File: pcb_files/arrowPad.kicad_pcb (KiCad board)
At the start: 2 copper layers, 76.2 x 64.8 mm, 30 parts, among them J1 AudioJack3_Ground, J2 AudioJack3_Ground, K1 KEYSW, K2 KEYSW, K3 KEYSW, K4 KEYSW, K5 KEYSW, K6 KEYSW, K7 KEYSW, K8 KEYSW, K9 KEYSW, U1 ProMicro, U2 NRF24L01_Breakout, U3 ADG417BN

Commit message: started reworking board
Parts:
- removed REF** (x4): MountingHole_3.5mm, MountingHole:MountingHole_3.5mm
- added U4: AMS1117-3.3, promicro:AMS1117flipped, F.Cu at (38.7, 90.8)
- J1, J2: footprint Connector_PinHeader_2.54mm:PinHeader_1x04_P2.54mm_Vertical -> SJ1-3514-SMT:CUI_SJ1-3514-SMT
- moved J1 15.8 mm to (38.1, 123.8), turned to 0 degrees
- moved J2 6.56 mm to (102.9, 128.9), turned to 180 degrees
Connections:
- U2 pad 2: Net-(J1-Pad3) -> Net-(U2-Pad2)
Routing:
- net Net-(J1-Pad2): track 145.8 -> 147.3 mm, vias 0 -> 2
- net Net-(J1-Pad1): track 151.5 -> 150.1 mm, vias 2 -> 0
- removed copper zone on F.Cu, net /GND1

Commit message: v2
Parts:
- removed J1, J2: AudioJack3_Ground, SJ1-3514-SMT:CUI_SJ1-3514-SMT
- removed R1: R, keyboard_parts:D_SOD123_axial
- added D11: D, keyboard_parts:D_SOD123_axial, F.Cu at (167.1, 112.6)
- added D12: D, keyboard_parts:D_SOD123_axial, F.Cu at (184.9, 112.0)
- added D13: D, keyboard_parts:D_SOD123_axial, F.Cu at (130.3, 131.1)
- added D14: D, keyboard_parts:D_SOD123_axial, F.Cu at (149.4, 131.7)
- added D15: D, keyboard_parts:D_SOD123_axial, F.Cu at (167.8, 132.3)
- added D16: D, keyboard_parts:D_SOD123_axial, F.Cu at (186.2, 131.1)
- added K10: KEYSW, keyswitches:PG1350_socket, F.Cu at (149.9, 102.9)
- added K11: KEYSW, keyswitches:PG1350_socket, F.Cu at (168.9, 102.9)
- added K12: KEYSW, keyswitches:PG1350_socket, F.Cu at (188.0, 102.9)
- added K13: KEYSW, keyswitches:PG1350_socket, F.Cu at (130.8, 121.9)
- added K14: KEYSW, keyswitches:PG1350_socket, F.Cu at (149.9, 121.9)
- added K15: KEYSW, keyswitches:PG1350_socket, F.Cu at (168.9, 121.9)
- added K16: KEYSW, keyswitches:PG1350_socket, F.Cu at (188.0, 121.9)
- D10: value LED -> D; footprint Connector_PinHeader_2.54mm:PinHeader_1x02_P2.54mm_Vertical -> keyboard_parts:D_SOD123_axial
- U1: footprint Transformer_SMD:proMicrov6 -> promicro:ProMicro
- moved K4 143.6 mm to (188.0, 64.8)
- moved D4 143.3 mm to (188.0, 74.9)
- moved BT1 126.4 mm to (179.1, 43.2)
- moved K8 126.0 mm to (188.0, 83.8)
- moved D7 125.7 mm to (169.0, 93.0)
- moved K7 125.5 mm to (168.9, 83.8)
- moved D8 124.2 mm to (186.2, 93.6)
- moved D10 107.5 mm to (148.7, 112.0), turned to 180 degrees
- moved U3 94.3 mm to (162.6, 54.6)
- moved D2 88.1 mm to (148.6, 61.0)
- moved D1 87.6 mm to (129.5, 61.0)
- moved K3 84.6 mm to (168.9, 64.8)
- moved D3 84.3 mm to (168.9, 74.9)
- moved K2 84.1 mm to (149.9, 64.8)
- moved K1 83.5 mm to (130.8, 64.8)
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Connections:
- net Net-(J1-Pad3) renamed /VCC1
- D10 pad 1: /GND1 -> /Row3
- D4 pad 1: /Row2 -> /Row1
- D7 pad 1: /Row3 -> /Row2
- D8 pad 1: /Row3 -> /Row2
- K4 pad 1: /Col1 -> /Col4
- K5 pad 1: /Col2 -> /Col1
- K6 pad 1: /Col3 -> /Col2
- K7 pad 1: /Col1 -> /Col3
- K8 pad 1: /Col2 -> /Col4
- K9 pad 1: /Col3 -> /Col1
- U1 pad 6: /Col1 -> Net-(J1-Pad2)
- U1 pad 7: Net-(R1-Pad1) -> /Col1
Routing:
- net Net-(U1-Pad1): track 150.1 -> 0.00 mm
- net Net-(U1-Pad2): track 147.3 -> 0.00 mm, vias 2 -> 0
- net /Col2: track 115.3 -> 0.00 mm, vias 5 -> 0
- net /Col1: track 100.8 -> 0.00 mm, vias 2 -> 0
- net /VCC1: track 90.8 -> 0.00 mm, vias 4 -> 0
- net /Row3: track 86.6 -> 0.00 mm, vias 1 -> 0
- net /RAW1: track 81.0 -> 0.00 mm, vias 1 -> 0
- net /Row2: track 56.4 -> 0.00 mm
- net Net-(R1-Pad1): track 49.9 -> 0.00 mm
- net /Col3: track 49.1 -> 0.00 mm, vias 3 -> 0
- net /Row1: track 47.5 -> 0.00 mm
- net Net-(U1-Pad18): track 23.8 -> 0.00 mm, vias 1 -> 0
- net Net-(U1-Pad15): track 22.6 -> 0.00 mm, vias 1 -> 0
- net Net-(U1-Pad17): track 22.3 -> 0.00 mm
- net Net-(U1-Pad16): track 21.3 -> 0.00 mm
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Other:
- board outline removed

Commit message: updated
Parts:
- moved BT1 28.7 mm to (151.1, 49.5)
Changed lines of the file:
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@@
   )
   (module Connector_PinHeader_2.54mm:PinHeader_1x02_P2.54mm_Vertical (layer F.Cu)
-    (at 179.07 43.18)
+    (at 151.13 49.53)
     (descr "Through hole straight pin header, 1x02, 2.54mm pitch, single row")
     (tags "Through hole pin header THT 1x02 2.54mm single row")

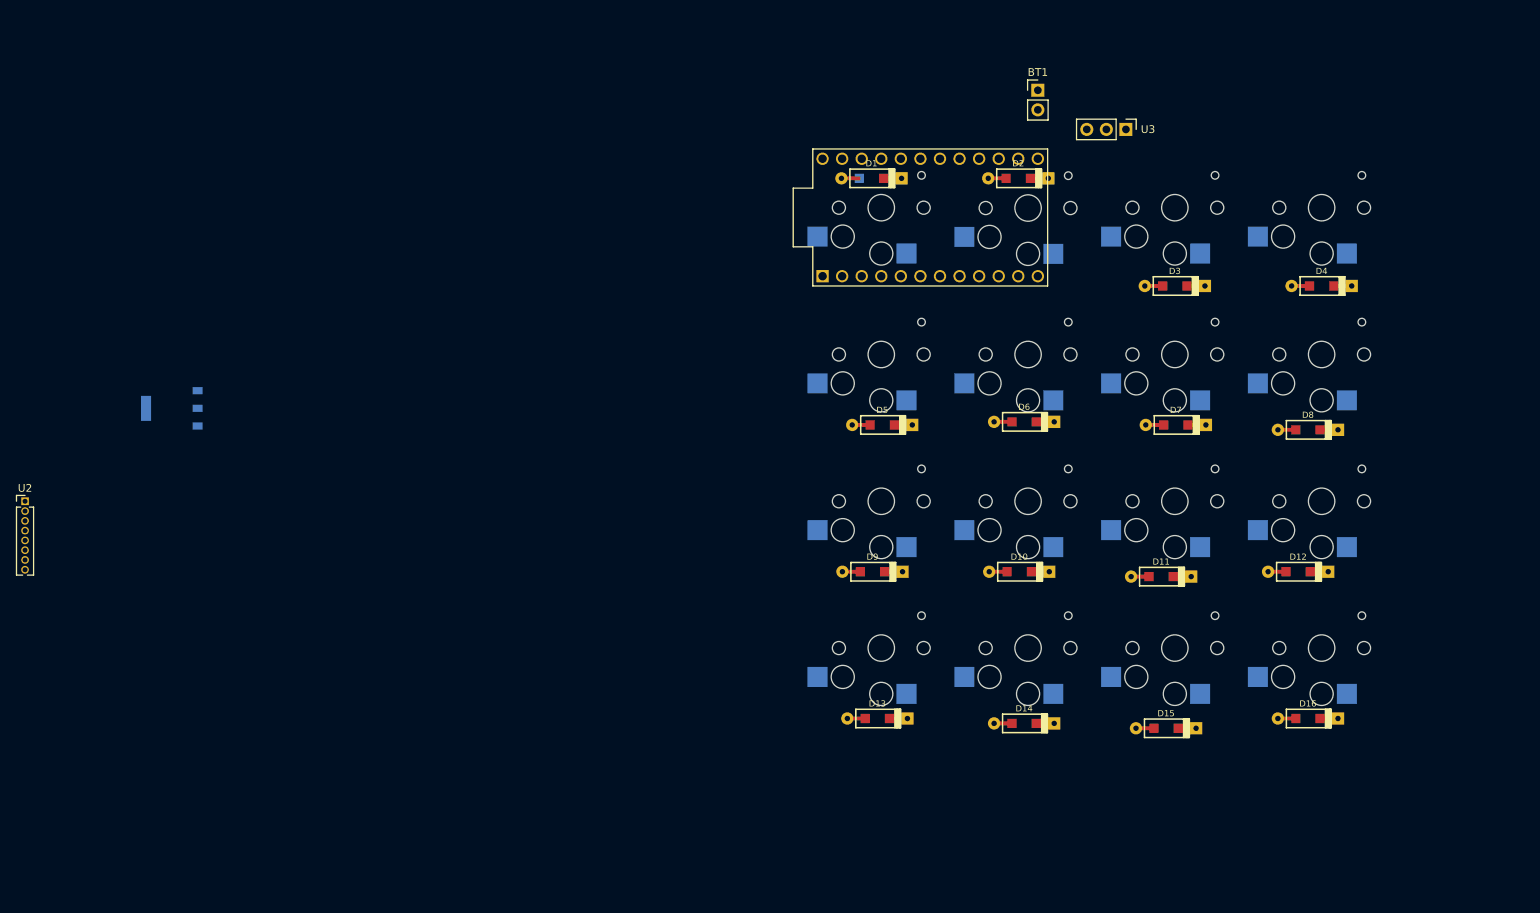
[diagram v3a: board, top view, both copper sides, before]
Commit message: switch and diode pcb layout
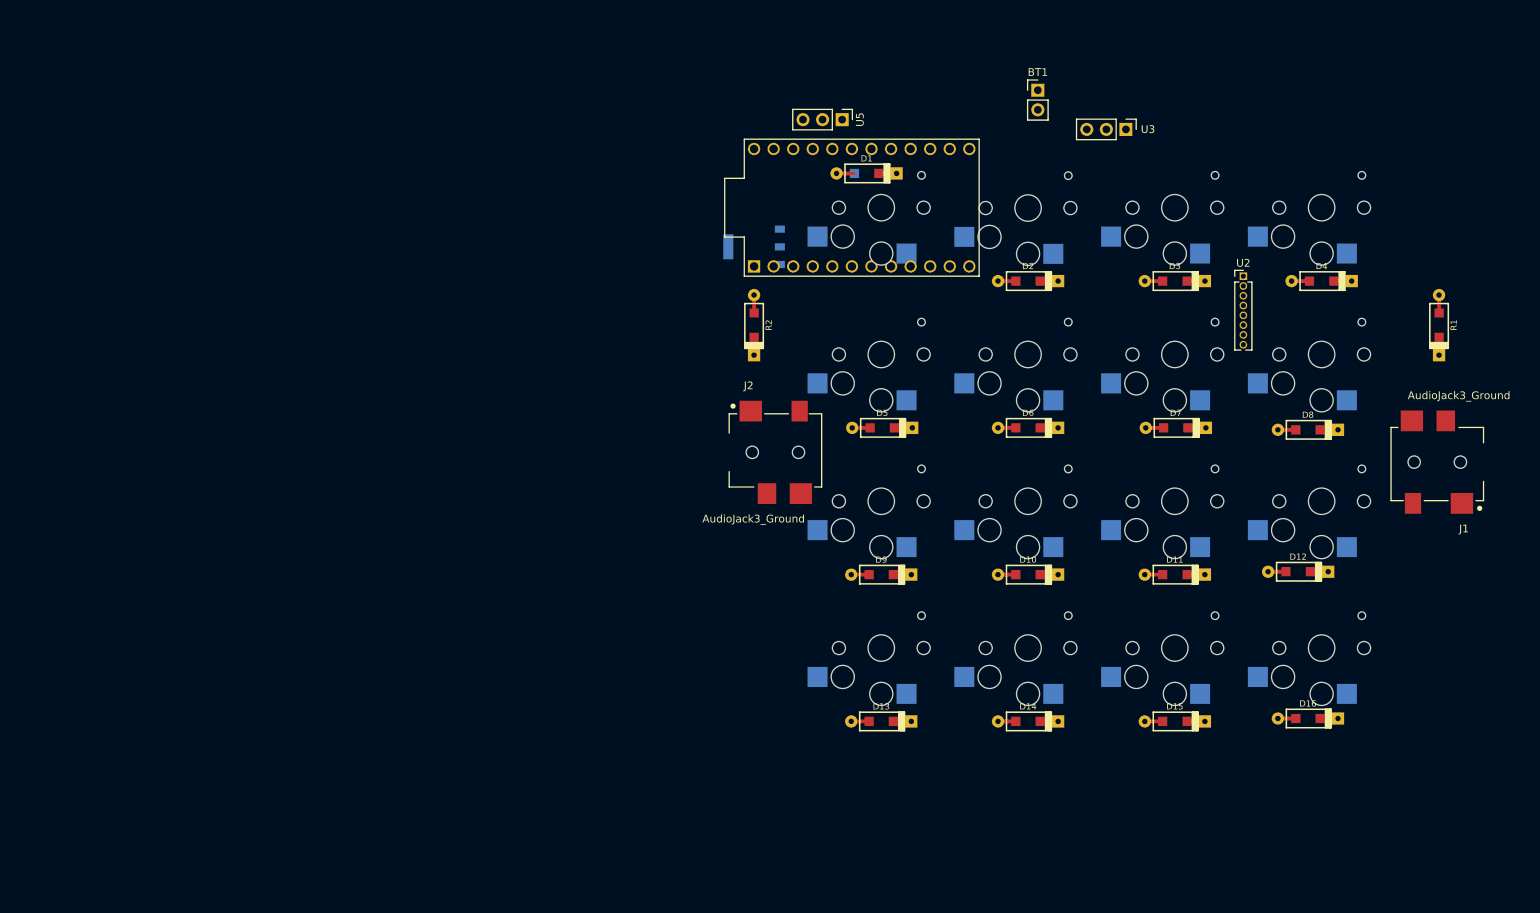
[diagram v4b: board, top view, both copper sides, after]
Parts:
- added J1: AudioJack3_Ground, foots:CUI_SJ1-3514-SMT[PAD1,2,34], F.Cu at (204.5, 97.8)
- added J2: AudioJack3_Ground, foots:CUI_SJ1-3514-SMT[PAD1,2,34], F.Cu at (115.6, 96.5)
- added R1: R, keyboard_parts:D_SOD123_axial, F.Cu at (203.2, 80.0)
- added R2: R, keyboard_parts:D_SOD123_axial, F.Cu at (114.3, 80.0)
- added U5: ADG417BN, Connector_PinHeader_2.54mm:PinHeader_1x03_P2.54mm_Vertical, F.Cu at (125.7, 53.3)
- moved U2 160.8 mm to (177.8, 73.7)
- moved U4 78.4 mm to (114.3, 69.8)
- moved D2 13.4 mm to (149.9, 74.3)
- moved U1 8.98 mm to (128.3, 64.8)
- moved D11 1.80 mm to (168.9, 112.4)
- moved D15 1.45 mm to (168.9, 131.4)
- moved D10 1.20 mm to (149.9, 112.4)
- moved D9 1.20 mm to (130.8, 112.4)
- moved D6 0.93 mm to (149.9, 93.3)
- moved D1 0.90 mm to (128.9, 60.3)
- moved D13 0.64 mm to (130.8, 131.4)
- moved D3 0.64 mm to (168.9, 74.3)
- moved D4 0.64 mm to (188.0, 74.3)
- moved D14 0.57 mm to (149.9, 131.4)
- moved D5 0.38 mm to (130.9, 93.3)
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
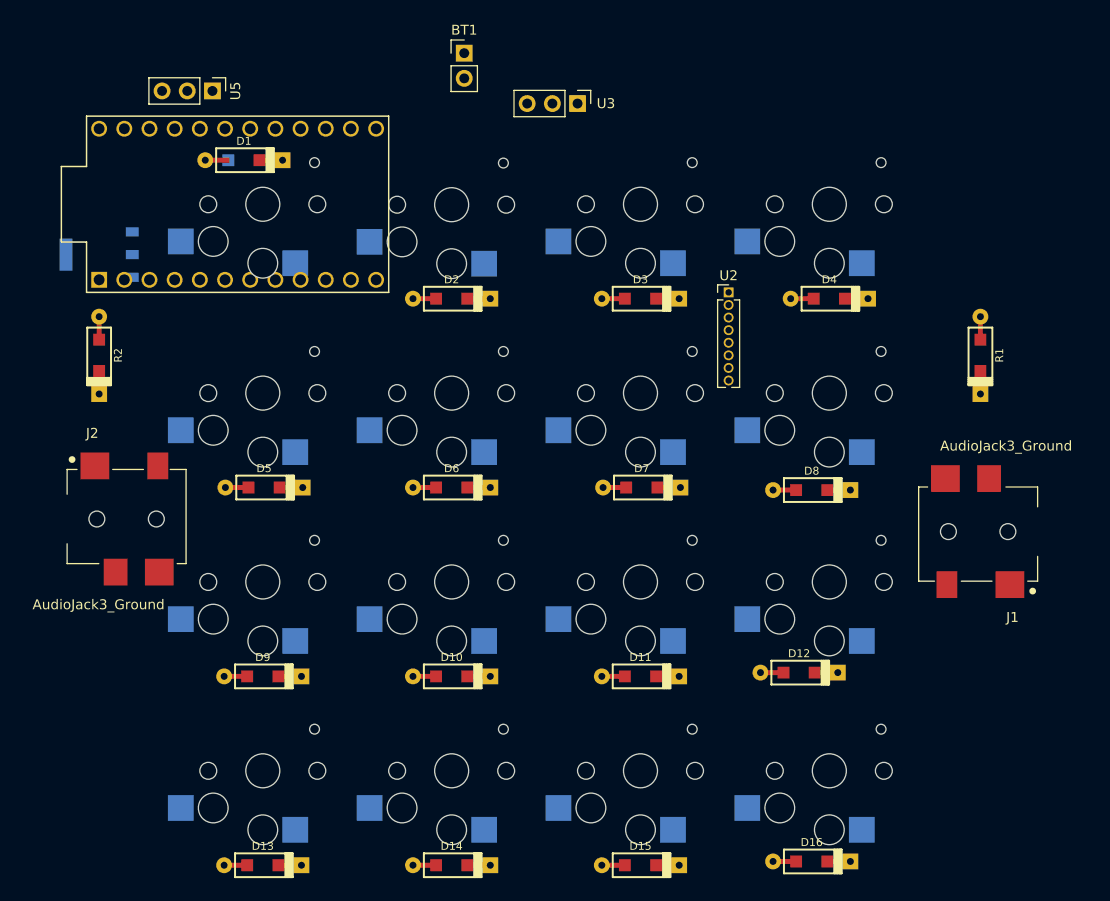
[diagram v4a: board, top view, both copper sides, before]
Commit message: layed out components
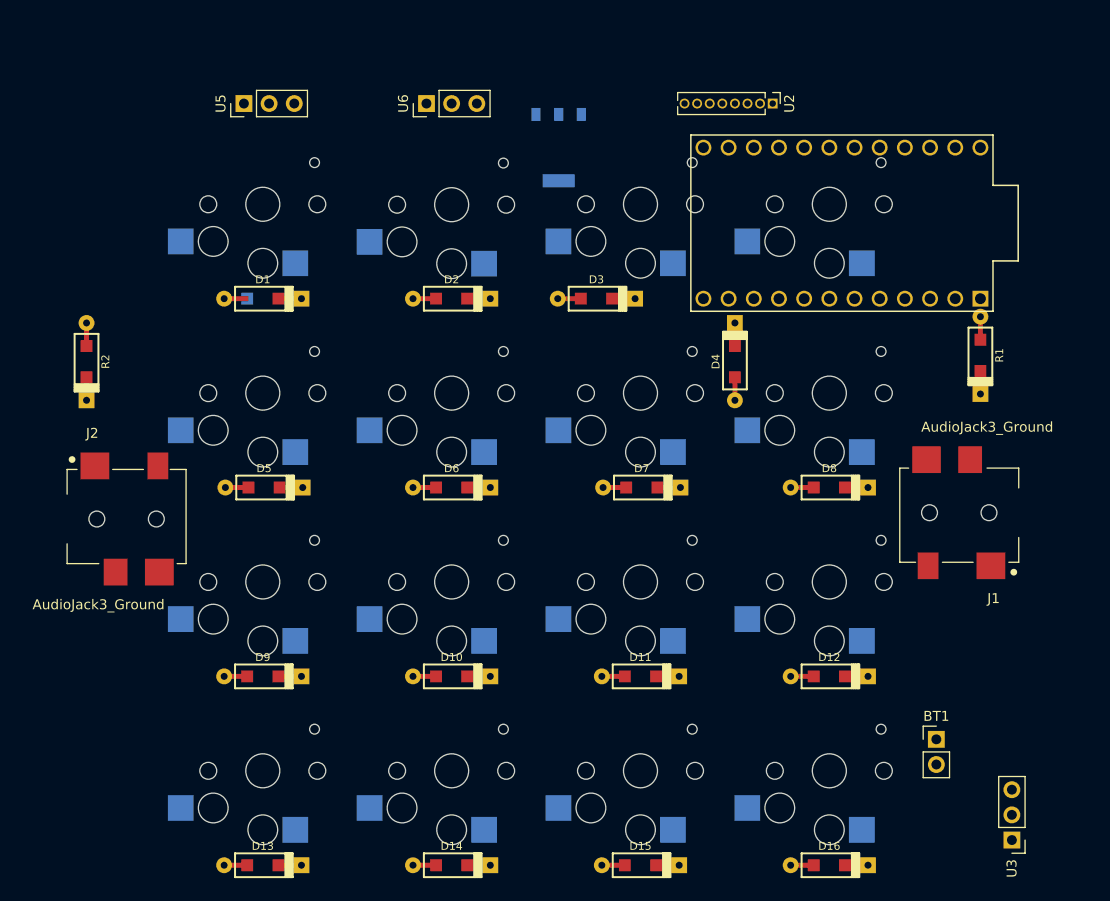
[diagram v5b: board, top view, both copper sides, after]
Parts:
- added U6: ADG417BN, Connector_PinHeader_2.54mm:PinHeader_1x03_P2.54mm_Vertical, F.Cu at (147.3, 54.6)
- U1: footprint promicro:ProMicro -> foots:ProMicroPinsFlipped
- moved U3 86.3 mm to (206.4, 128.9), turned to 180 degrees
- moved BT1 84.0 mm to (198.8, 118.7)
- moved U1 61.0 mm to (189.2, 66.7), turned to 180 degrees
- moved U4 47.6 mm to (160.7, 59.1), turned to 180 degrees
- moved U2 19.6 mm to (182.2, 54.6), turned to 270 degrees
- moved D1 14.1 mm to (130.8, 74.3)
- moved D4 11.4 mm to (178.4, 80.6), turned to 270 degrees
- moved D3 4.44 mm to (164.5, 74.3)
- moved U5 3.42 mm to (128.9, 54.6), turned to 90 degrees
- moved D12 3.07 mm to (188.0, 112.4)
- moved J1 2.69 mm to (202.6, 95.9)
- moved D16 1.82 mm to (188.0, 131.4)
- moved D8 1.80 mm to (188.0, 93.3)
- moved R2 1.42 mm to (113.0, 80.6)
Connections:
- U4 pad 3: /VCC1 -> Net-(U4-Pad3)
